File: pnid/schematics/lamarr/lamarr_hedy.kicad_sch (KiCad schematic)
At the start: 101 parts

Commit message: updated PNID
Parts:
- added ox_pressure_reducer_pressure: ox_pressure_reducer_pressure:sensor, symbol PnID-Lib:Sensor_Pressure
- engine_ECU_temperature: value engine_temp_1:sensor -> engine_temp_0:sensor
- renumbered fuel_main_valve_temperature to ox_decoupler_temperature, burst_disk_temperature to ox_press_temp
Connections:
- net at engine.~ (C): now also venturi1.~; no longer ox_venturi.~
- net at venturi1.~: now also fuel_main_valve.~, fuel_venturi_pressure.~; no longer engine.~ (C)
- net at dewar_needle_valve?.~: now also C2.~, C3.~; no longer C1.~
- net at Orifice2.~: now also fuel_pressurant_valve.~, pressurantPressureRegulator1.~
- new net: engine.~ (C), ox_venturi.~
- new net: OX.~, ox_main_valve.~, ox_quick_connect.~
- new net: DewarOverPressureValve?.~, LOX.~, dewar_pressurize_solenoid.~
- new net: C1.~, dewar_needle_valve?.~
- new net: Orifice1.~, ox_pressurant_valve.~, ox_pressure_reducer_pressure.~, pressurantPressureRegulator2.~
- new net: FUEL.~, fuel_main_valve.~, ox_quick_connect1.~
- now unconnected: Orifice1.~
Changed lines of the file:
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@@
 	)
 	(junction
+		(at 120.904 76.2)
+		(diameter 0)
+		(color 0 0 0 0)
+	)
+	(junction
 		(at 78.486 74.676)
 		(diameter 0)
@@
 	(wire
 		(pts
+			(xy 120.904 76.2) (xy 120.904 77.47)
+		)
+		(stroke
+			(width 0)
+			(type default)
+		)
+	)
+	(wire
+		(pts
 			(xy 95.758 193.04) (xy 95.758 198.12)
 		)
@@
 	(wire
 		(pts
-			(xy 90.17 147.32) (xy 83.82 147.32)
-		)
-		(stroke
-			(width 0)
-			(type default)
-		)
-	)
-	(wire
-		(pts
 			(xy 21.59 56.134) (xy 28.194 56.134)
 		)
@@
 	(wire
 		(pts
-			(xy 83.82 147.32) (xy 83.82 151.13)
+			(xy 154.94 127) (xy 154.94 147.32)
 		)
 		(stroke
@@
 	(wire
 		(pts
-			(xy 81.28 151.13) (xy 83.82 151.13)
-		)
-		(stroke
-			(width 0)
-			(type default)
-		)
-	)
-	(wire
-		(pts
 			(xy 78.486 45.974) (xy 78.486 49.53)
 		)
@@
 	(wire
 		(pts
-			(xy 120.904 74.676) (xy 120.904 77.47)
+			(xy 120.904 74.676) (xy 120.904 76.2)
 		)
 		(stroke
@@
 	(wire
 		(pts
-			(xy 163.83 147.32) (xy 155.956 147.32)
+			(xy 155.956 147.32) (xy 163.83 147.32)
 		)
 		(stroke
@@
 	(wire
 		(pts
+			(xy 130.81 76.2) (xy 120.904 76.2)
+		)
+		(stroke
+			(width 0)
+			(type default)
+		)
+	)
+	(wire
+		(pts
 			(xy 120.904 87.63) (xy 120.904 91.44)
 		)
@@
 	(symbol
 		(lib_id "PnID-Lib:Sensor_Temperature")
-		(at 134.62 95.25 0)
+		(at 134.62 22.86 0)
 		(unit 1)
 		(exclude_from_sim no)
@@
 		(on_board yes)
 		(dnp no)
-		(property "Reference" "burst_disk_temperature"
-			(at 138.43 94.615 0)
+		(property "Reference" "ox_press_temp"
+			(at 138.43 22.225 0)
 			(effects
 				(font
@@
 		)
 		(property "Value" "ox_temp_0:sensor"
-			(at 135.636 90.17 0)
+			(at 135.636 17.78 0)
 			(effects
 				(font
@@
 		)
 		(property "Footprint" ""
-			(at 134.62 95.25 0)
+			(at 134.62 22.86 0)
 			(effects
 				(font
@@
 		)
 		(property "Datasheet" ""
-			(at 134.62 95.25 0)
+			(at 134.62 22.86 0)
 			(effects
 				(font
@@
 		)
 		(property "Description" ""
-			(at 134.62 95.25 0)
+			(at 134.62 22.86 0)
 			(effects
 				(font
@@
 		)
 		(property "Unit" "˚C"
-			(at 134.62 95.25 0)
+			(at 134.62 22.86 0)
 			(effects
 				(font
@@
 		)
 		(property "Action_Reference" " "
-			(at 134.62 95.25 0)
+			(at 134.62 22.86 0)
 			(effects
 				(font
@@
 			(project "lamarr_hedy"
 				(path "/604fc9f3-63a6-4133-afd1-4a5c2507dc1d"
-					(reference "burst_disk_temperature")
+					(reference "ox_press_temp")
 					(unit 1)
 				)
@@
 	)
 	(symbol
+		(lib_id "PnID-Lib:Sensor_Pressure")
+		(at 138.43 76.2 0)
+		(unit 1)
+		(exclude_from_sim no)
+		(in_bom yes)
+		(on_board yes)
+		(dnp no)
+		(property "Reference" "ox_pressure_reducer_pressure"
+			(at 141.6812 74.4982 0)
+			(effects
+				(font
+					(size 0.508 0.508)
+				)
+				(justify left)
+				(hide yes)
+			)
+		)
+		(property "Value" "ox_pressure_reducer_pressure:sensor"
+			(at 142.24 76.2 0)
+			(effects
+				(font
+					(size 0.508 0.508)
+				)
+				(justify left)
+			)
+		)
+		(property "Footprint" ""
+			(at 138.43 76.2 0)
+			(effects
+				(font
+					(size 0.508 0.508)
+				)
+				(hide yes)
+			)
+		)
+		(property "Datasheet" ""
+			(at 138.43 76.2 0)
+			(effects
+				(font
+					(size 0.508 0.508)
+				)
+				(hide yes)
+			)
+		)
+		(property "Description" ""
+			(at 138.43 76.2 0)
+			(effects
+				(font
+					(size 1.27 1.27)
+				)
+				(hide yes)
+			)
+		)
+		(property "Unit" "bar"
+			(at 138.43 76.2 0)
+			(effects
+				(font
+					(size 0.508 0.508)
+				)
+				(hide yes)
+			)
+		)
+		(property "Action_Reference" " "
+			(at 138.43 76.2 0)
+			(effects
+				(font
+					(size 1.27 1.27)
+				)
+				(hide yes)
+			)
+		)
+		(property "Data_Content" " "
+			(at 141.6812 77.2922 0)
+			(effects
+				(font
+					(size 1.27 1.27)
+				)
+				(justify left)
+				(hide yes)
+			)
+		)
+		(pin "~"
+		)
+		(instances
+			(project "lamarr_hedy"
+				(path "/604fc9f3-63a6-4133-afd1-4a5c2507dc1d"
+					(reference "ox_pressure_reducer_pressure")
+					(unit 1)
+				)
+			)
+		)
+	)
+	(symbol
 		(lib_id "PnID-Lib:voltmeter")
 		(at 110.998 198.12 0)
@@
 			)
 		)
-		(property "Value" "engine_temp_1:sensor"
+		(property "Value" "engine_temp_0:sensor"
 			(at 153.289 183.134 0)
 			(effects
@@
 		(lib_name "Sensor_Temperature_1")
 		(lib_id "PnID-Lib:Sensor_Temperature")
-		(at 97.79 147.32 0)
+		(at 162.56 127 0)
 		(unit 1)
 		(exclude_from_sim no)
@@
 		(on_board yes)
 		(dnp no)
-		(property "Reference" "fuel_main_valve_temperature"
-			(at 101.6 146.685 0)
+		(property "Reference" "ox_decoupler_temperature"
+			(at 166.37 126.365 0)
 			(effects
 				(font
@@
 		)
 		(property "Value" "engine_temp_0:sensor"
-			(at 94.996 142.494 0)
+			(at 166.878 127 0)
 			(effects
 				(font
@@
 		)
 		(property "Footprint" ""
-			(at 97.79 147.32 0)
+			(at 162.56 127 0)
 			(effects
 				(font
@@
 		)
 		(property "Datasheet" ""
-			(at 97.79 147.32 0)
+			(at 162.56 127 0)
 			(effects
 				(font
@@
 		)
 		(property "Description" ""
-			(at 97.79 147.32 0)
+			(at 162.56 127 0)
 			(effects
 				(font
@@
 		)
 		(property "Unit" "˚C"
-			(at 97.79 147.32 0)
+			(at 162.56 127 0)
 			(effects
 				(font
@@
 		)
 		(property "Action_Reference" " "
-			(at 97.79 147.32 0)
+			(at 162.56 127 0)
 			(effects
 				(font
@@
 			(project "lamarr_hedy"
 				(path "/604fc9f3-63a6-4133-afd1-4a5c2507dc1d"
-					(reference "fuel_main_valve_temperature")
+					(reference "ox_decoupler_temperature")
 					(unit 1)
 				)

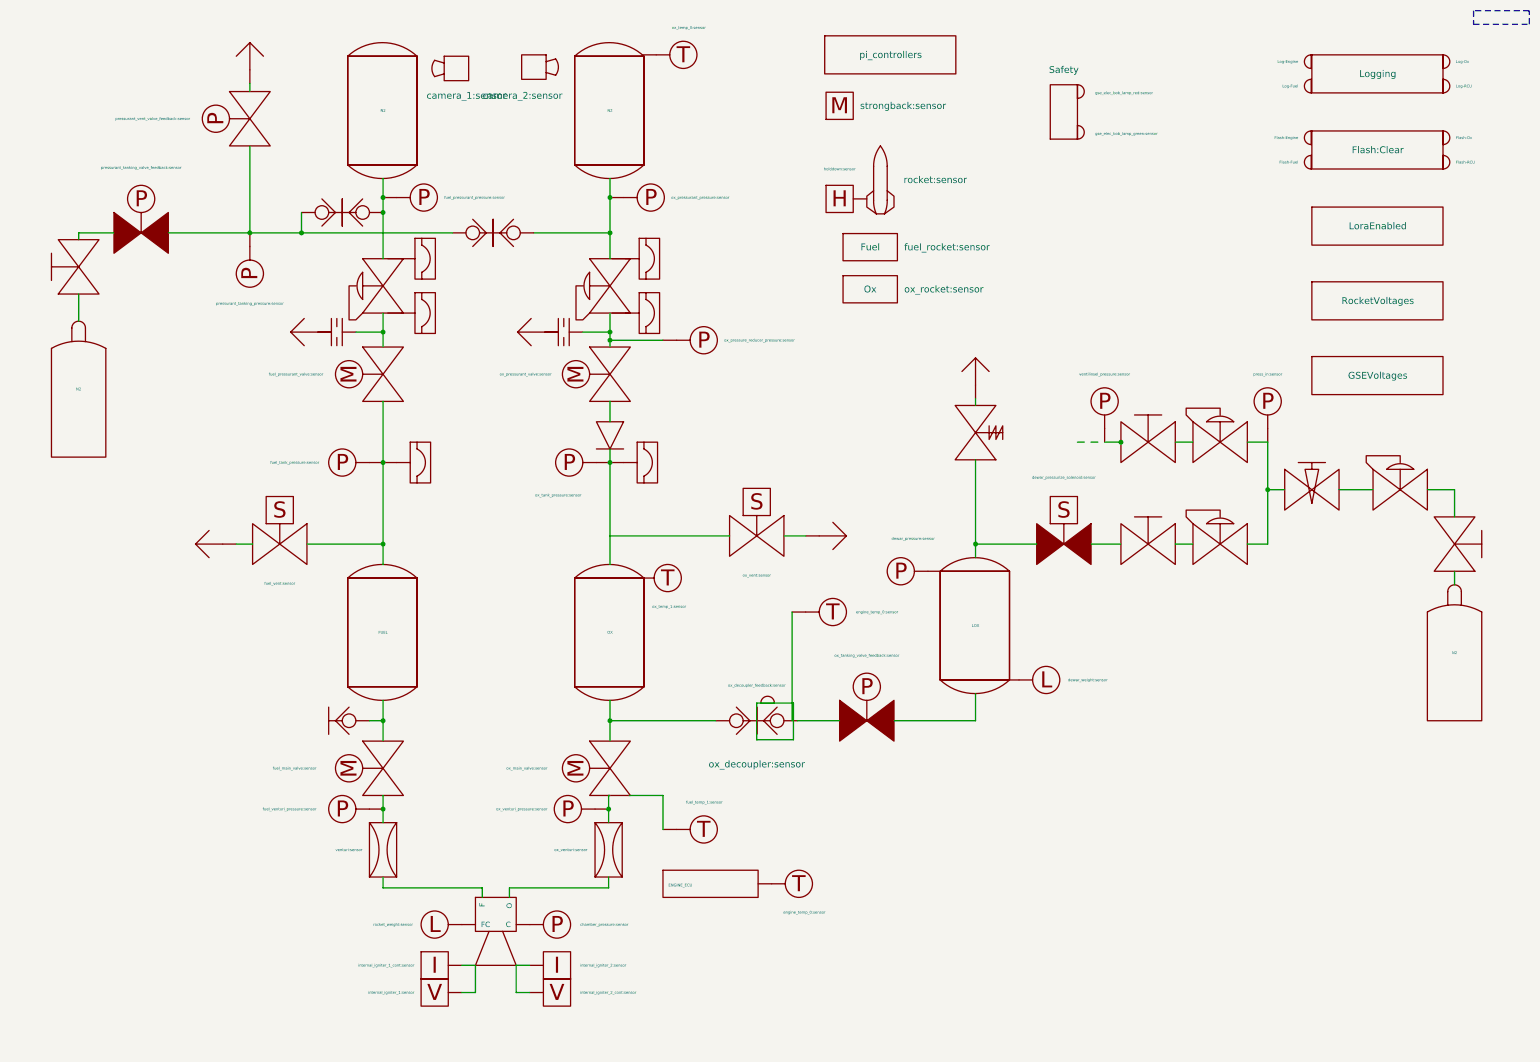
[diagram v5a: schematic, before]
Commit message: Added fuel/ox pressurant vent to the pnid & mapping Added servo controlled throttle to the pnid & mapping
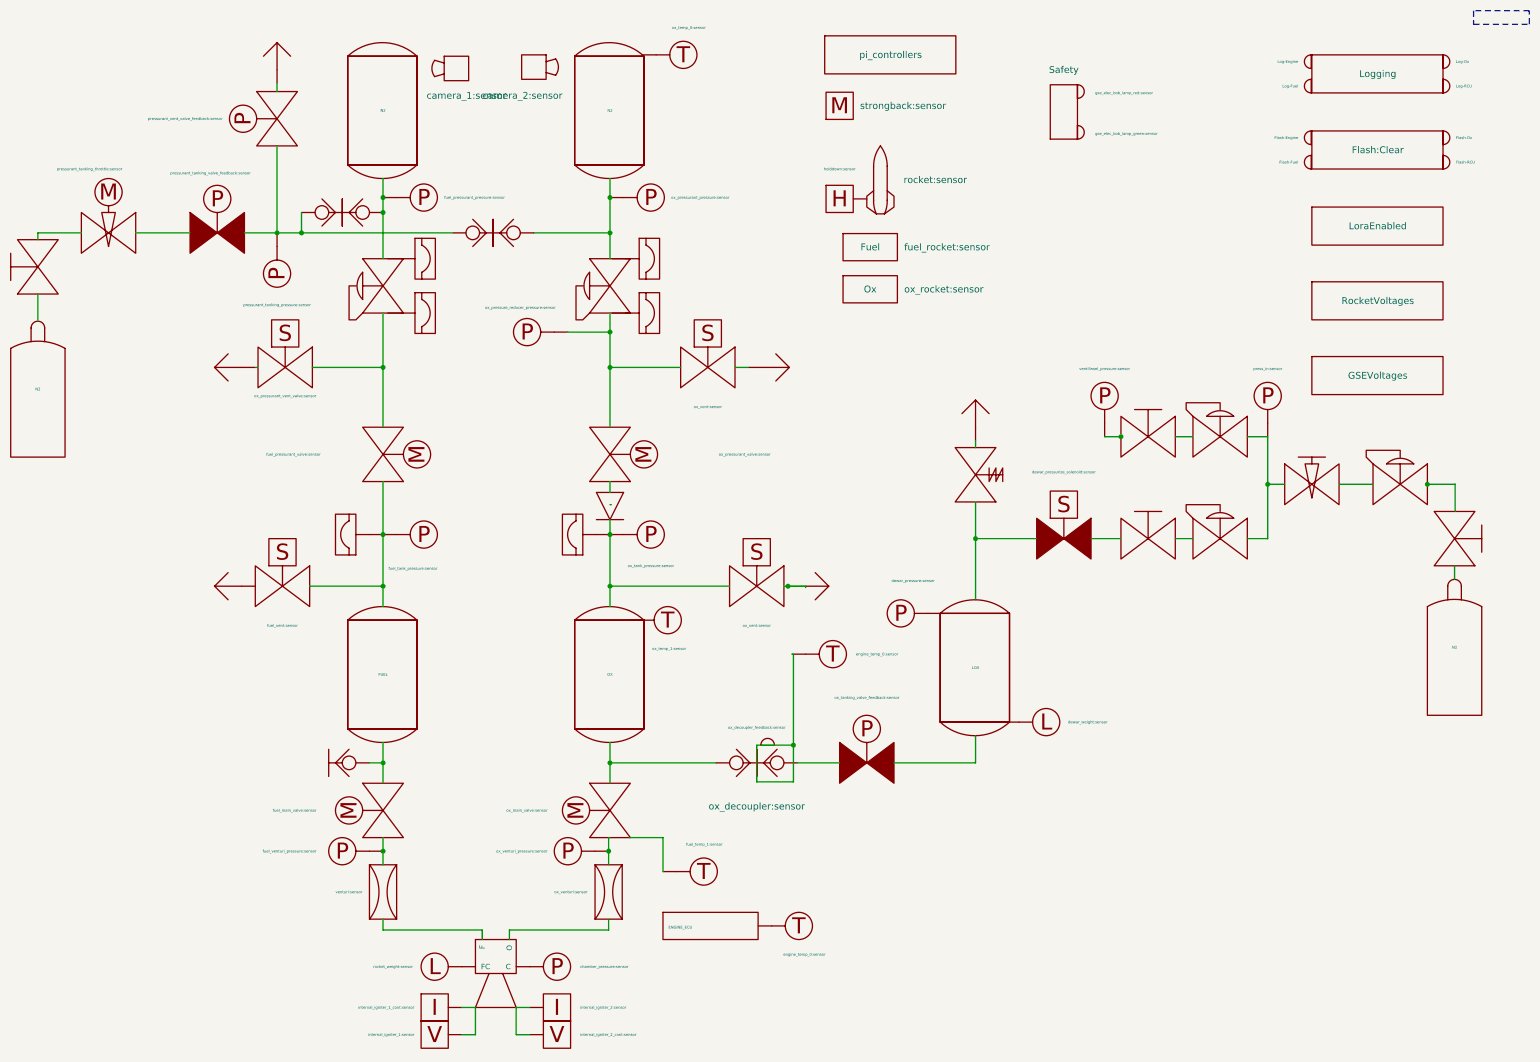
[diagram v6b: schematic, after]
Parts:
- removed Orifice1, Orifice2: Orifice, symbol PnID-Lib:Orifice
- added ox_pressurant_vent_valve: ox_pressurant_vent_valve:sensor, symbol PnID-Lib:Valve_Solenoid_NO
- added ox_vent1: ox_vent:sensor, symbol PnID-Lib:Valve_Solenoid_NO
- added pressurant_tanking_throttle: pressurant_tanking_throttle:sensor, symbol PnID-Lib:Valve_Needle_Servo
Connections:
- net at engine.~ (C): now also venturi1.~; no longer ox_venturi.~
- net at venturi1.~: now also fuel_main_valve.~, fuel_venturi_pressure.~; no longer engine.~ (C)
- net at dewar_needle_valve?.~: now also C2.~, C3.~; no longer C1.~
- net at C1.~: no longer dewar_manual_valve?.~
- net at pressurant_tanking_valve_(A1).~: now also pressurant_tanking_throttle.~; no longer dewar_manual_valve1.~
- net at ox_pressurant_valve.~, ox_pressure_reducer_pressure.~, pressurantPressureRegulator2.~: now also ox_vent1.~
- net at BurstDisc1.~, CheckValve2.~, OX.~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: now also ox_vent.~
- net at fuel_pressurant_valve.~, pressurantPressureRegulator1.~: now also ox_pressurant_vent_valve.~
- net at Vent4.~: now also ox_vent1.~
- net at Vent5.~: now also ox_pressurant_vent_valve.~
- new net: engine.~ (C), ox_venturi.~
- new net: OX.~, ox_main_valve.~, ox_quick_connect.~
- new net: DewarOverPressureValve?.~, LOX.~, dewar_pressurize_solenoid.~
- new net: C1.~, dewar_needle_valve?.~
- new net: FUEL.~, fuel_main_valve.~, ox_quick_connect1.~
- new net: dewar_manual_valve1.~, pressurant_tanking_throttle.~
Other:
- moved on the sheet: FUEL, LOX, N2, OX

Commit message: Static fire 25.8.2025 setup. Changes were not reviewd by me (raffael rott)
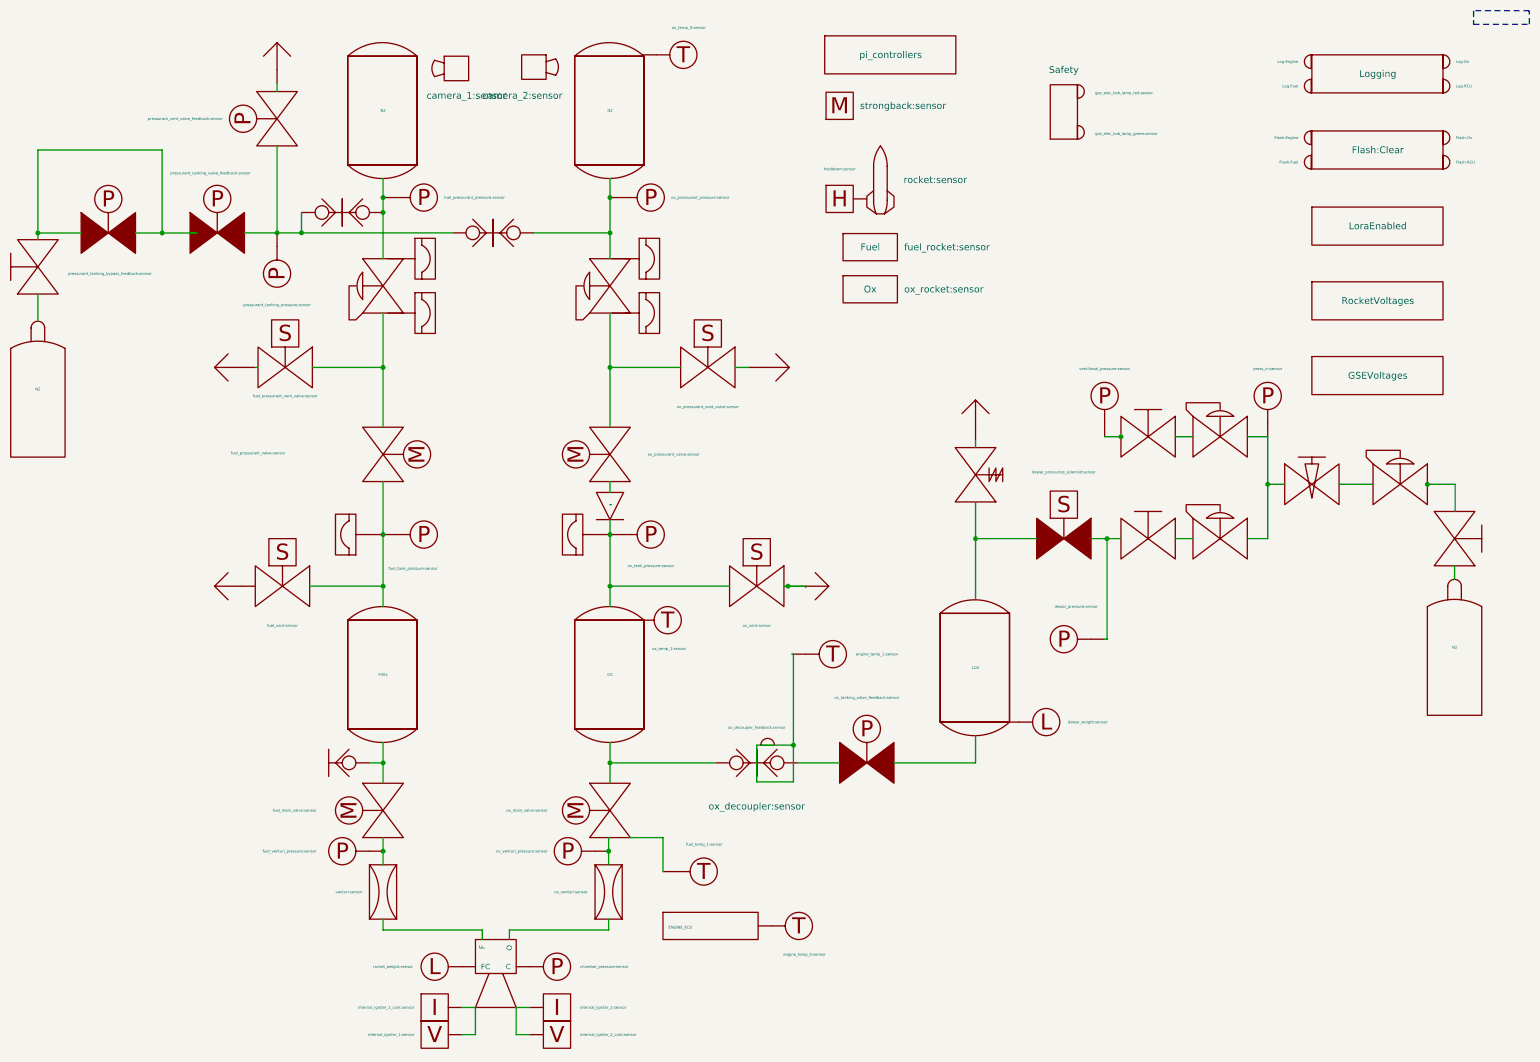
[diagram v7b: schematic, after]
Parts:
- removed ox_pressure_reducer_pressure: ox_pressure_reducer_pressure:sensor, symbol PnID-Lib:Sensor_Pressure
- removed pressurant_tanking_throttle: pressurant_tanking_throttle:sensor, symbol PnID-Lib:Valve_Needle_Servo
- added pressurant_tanking_bypass: pressurant_tanking_bypass_feedback:sensor, symbol PnID-Lib:Valve_Pneumatic
- fuel_pressurant_vent_valve: renamed from ox_pressurant_vent_valve; value ox_pressurant_vent_valve:sensor -> fuel_pressurant_vent_valve:sensor
- ox_decoupler_temperature: value engine_temp_0:sensor -> engine_temp_1:sensor
- ox_pressurant_vent_valve: renamed from ox_vent1; value ox_vent:sensor -> ox_pressurant_vent_valve:sensor
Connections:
- net at engine.~ (C): now also venturi1.~; no longer ox_venturi.~
- net at venturi1.~: now also fuel_main_valve.~, fuel_venturi_pressure.~; no longer engine.~ (C)
- net at C4.~, dewar_pressurize_solenoid.~: now also dewar_pressure.~
- net at dewar_needle_valve?.~: now also C2.~, C3.~; no longer C1.~
- net at pressurant_tanking_valve_(A1).~: now also dewar_manual_valve1.~, pressurant_tanking_bypass.~
- net at dewar_manual_valve1.~: now also N2.~
- new net: engine.~ (C), ox_venturi.~
- new net: OX.~, ox_main_valve.~, ox_quick_connect.~
- new net: DewarOverPressureValve?.~, LOX.~, dewar_pressurize_solenoid.~
- new net: C1.~, dewar_needle_valve?.~
- new net: ox_pressurant_valve.~, ox_pressurant_vent_valve.~, pressurantPressureRegulator2.~
- new net: FUEL.~, fuel_main_valve.~, ox_quick_connect1.~
